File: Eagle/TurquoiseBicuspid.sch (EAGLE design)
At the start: 7 parts

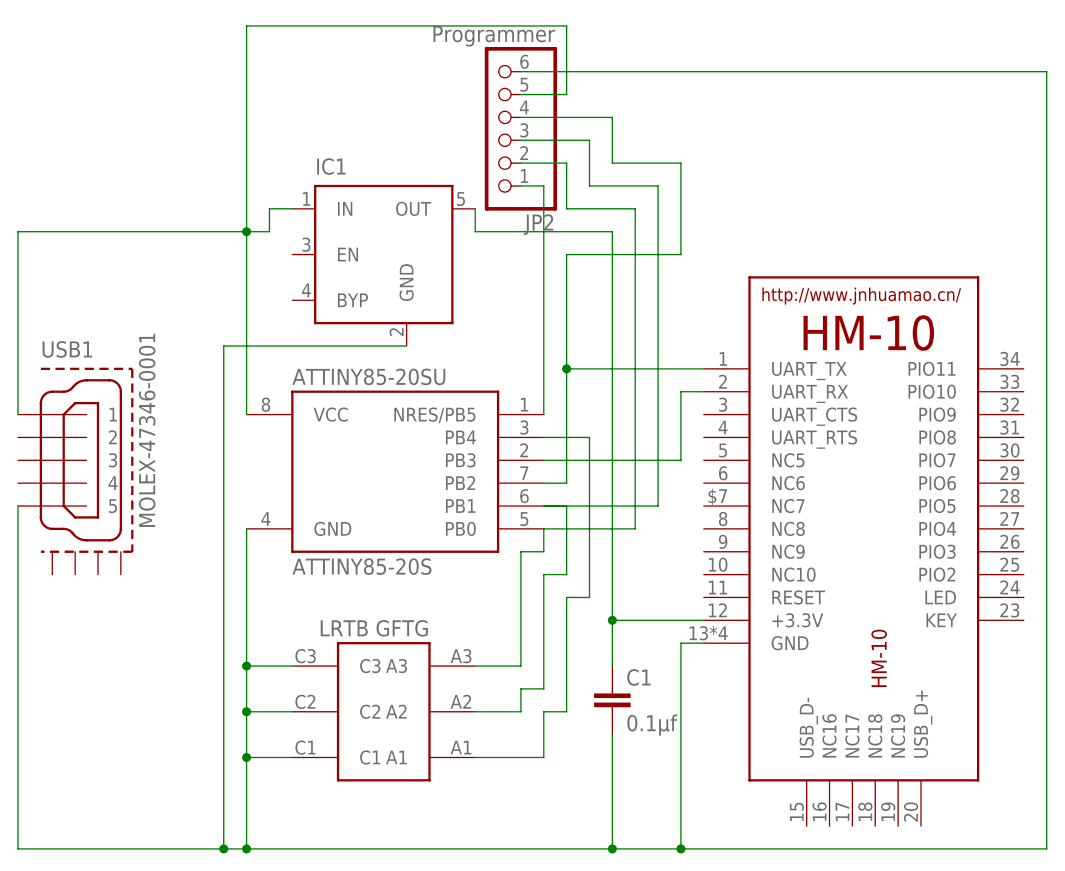
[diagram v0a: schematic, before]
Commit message: added resistors and switches
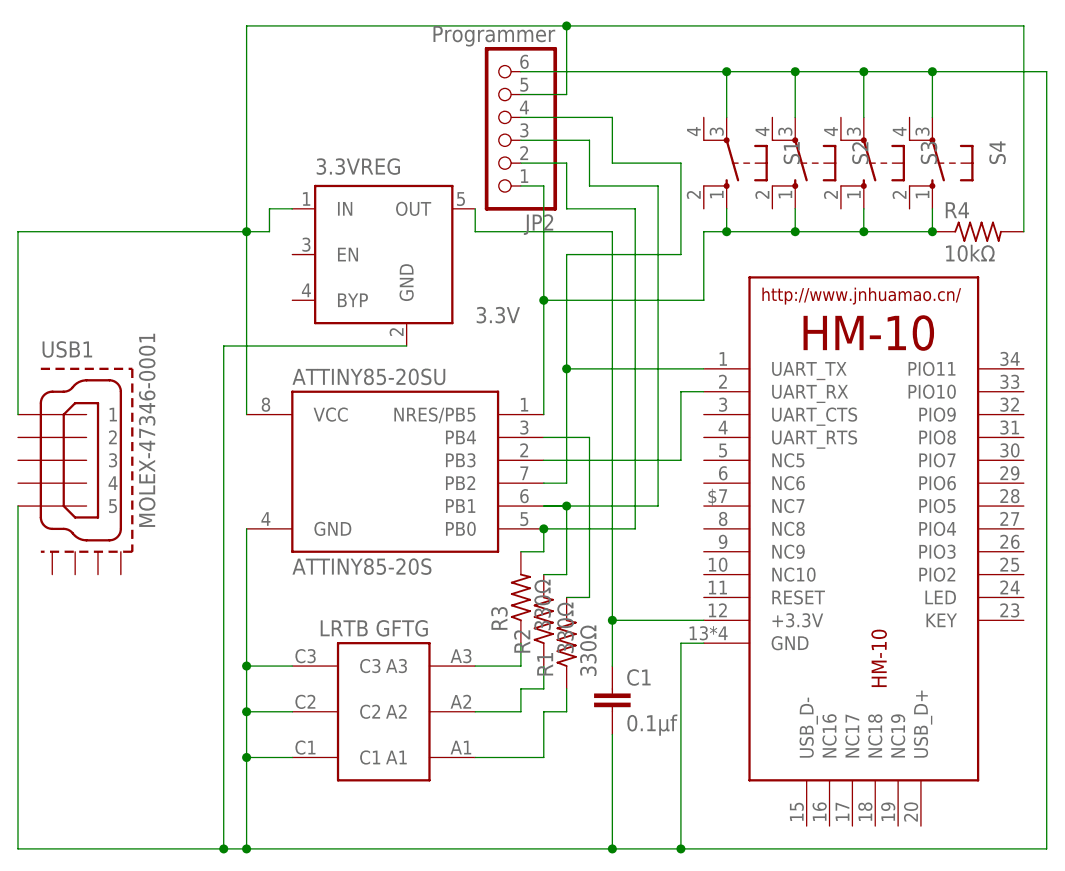
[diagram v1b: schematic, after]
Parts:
- added R1, R2, R3: 330Ω, rcl:R-US_M1206
- added R4: 10kΩ, rcl:R-US_R1206
- added S1, S2, S3, S4: (no value), switch-omron:10-XX
- 3.3VREG: value (none) -> 3.3V
- renumbered IC1 to 3.3VREG
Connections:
- new net N$7: R3.1, U$1.A3
- new net N$8: R2.1, U$1.A2
- new net N$9: R1.1, U$1.A1
- net 5V: now also R4.2
- net GND: now also S1.P, S2.P, S3.P, S4.P
- net N$1: now also R3.2; no longer U$1.A3
- net N$2: now also R2.2; no longer U$1.A2
- net N$3: now also R1.2; no longer U$1.A1
- net N$4: now also R4.1, S1.S, S2.S, S3.S, S4.S

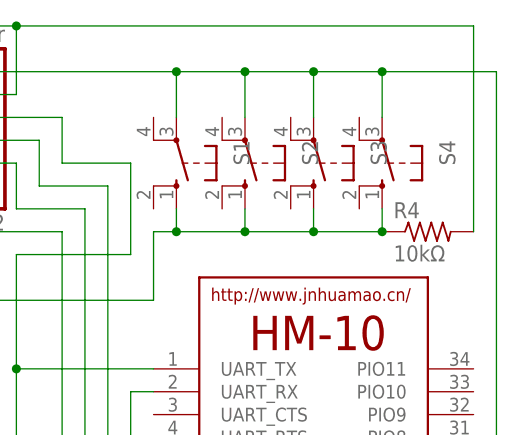
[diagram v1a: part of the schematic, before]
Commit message: removed 1 switch
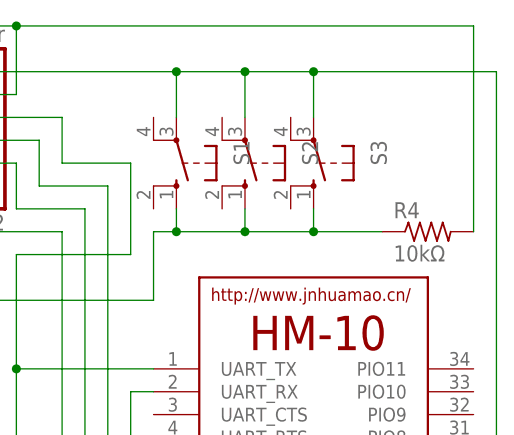
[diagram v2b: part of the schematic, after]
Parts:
- removed S4: (no value), switch-omron:10-XX
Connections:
- net GND: no longer S4.P
- net N$4: no longer S4.S
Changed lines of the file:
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@@
 <part name="S2" library="switch-omron" deviceset="10-XX" device=""/>
 <part name="S3" library="switch-omron" deviceset="10-XX" device=""/>
-<part name="S4" library="switch-omron" deviceset="10-XX" device=""/>
 </parts>
 <sheets>
@@
 <instance part="S2" gate="1" x="45.72" y="50.8" rot="R180"/>
 <instance part="S3" gate="1" x="53.34" y="50.8" rot="R180"/>
-<instance part="S4" gate="1" x="60.96" y="50.8" rot="R180"/>
 </instances>
 <busses>
@@
 <wire x1="38.1" y1="60.96" x2="45.72" y2="60.96" width="0.1524" layer="91"/>
 <wire x1="45.72" y1="60.96" x2="53.34" y2="60.96" width="0.1524" layer="91"/>
-<wire x1="53.34" y1="60.96" x2="60.96" y2="60.96" width="0.1524" layer="91"/>
-<wire x1="60.96" y1="60.96" x2="73.66" y2="60.96" width="0.1524" layer="91"/>
+<wire x1="53.34" y1="60.96" x2="73.66" y2="60.96" width="0.1524" layer="91"/>
 <wire x1="73.66" y1="60.96" x2="73.66" y2="-25.4" width="0.1524" layer="91"/>
 <pinref part="S1" gate="1" pin="P"/>
@@
 <pinref part="S3" gate="1" pin="P"/>
 <wire x1="53.34" y1="55.88" x2="53.34" y2="60.96" width="0.1524" layer="91"/>
-<pinref part="S4" gate="1" pin="P"/>
-<wire x1="60.96" y1="55.88" x2="60.96" y2="60.96" width="0.1524" layer="91"/>
 <junction x="38.1" y="60.96"/>
 <junction x="45.72" y="60.96"/>
 <junction x="53.34" y="60.96"/>
-<junction x="60.96" y="60.96"/>
 </segment>
 </net>
@@
 <pinref part="S3" gate="1" pin="S"/>
 <wire x1="53.34" y1="43.18" x2="53.34" y2="45.72" width="0.1524" layer="91"/>
-<pinref part="S4" gate="1" pin="S"/>
-<wire x1="60.96" y1="43.18" x2="60.96" y2="45.72" width="0.1524" layer="91"/>
-<junction x="60.96" y="43.18"/>
 <junction x="53.34" y="43.18"/>
 <junction x="45.72" y="43.18"/>

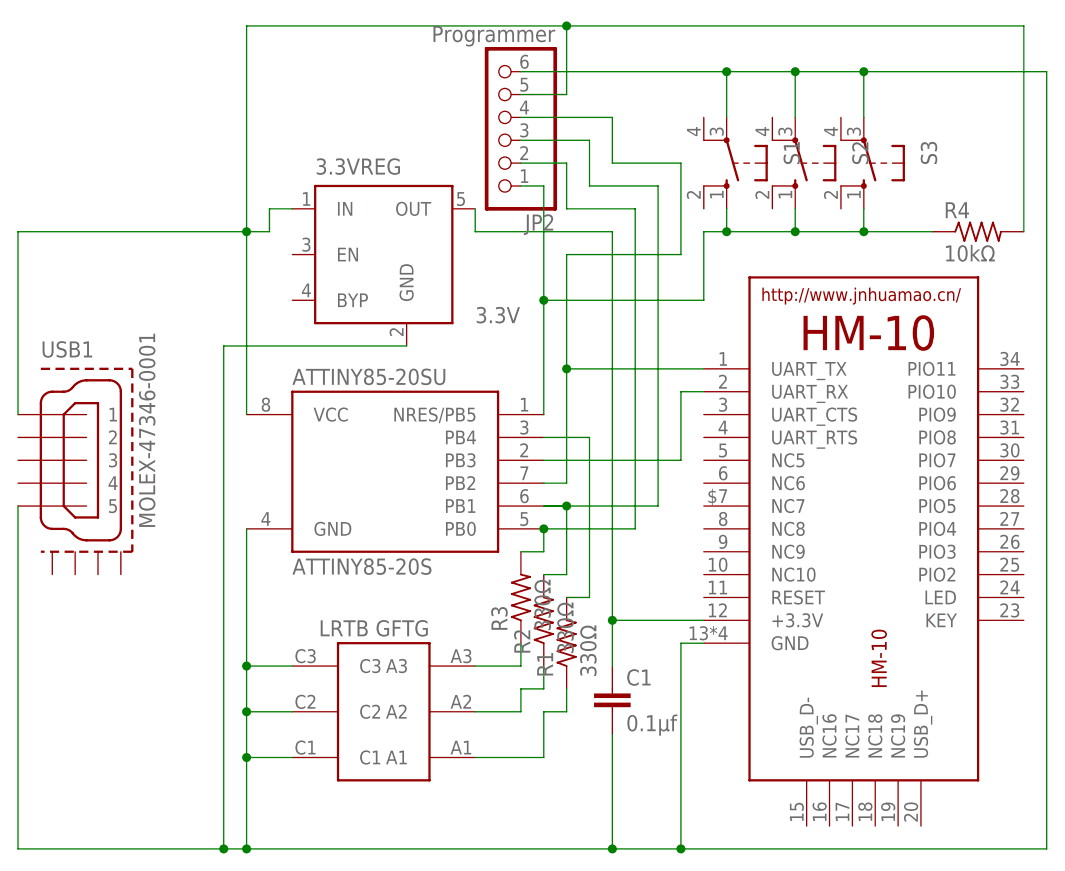
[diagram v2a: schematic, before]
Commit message: removed programming headers
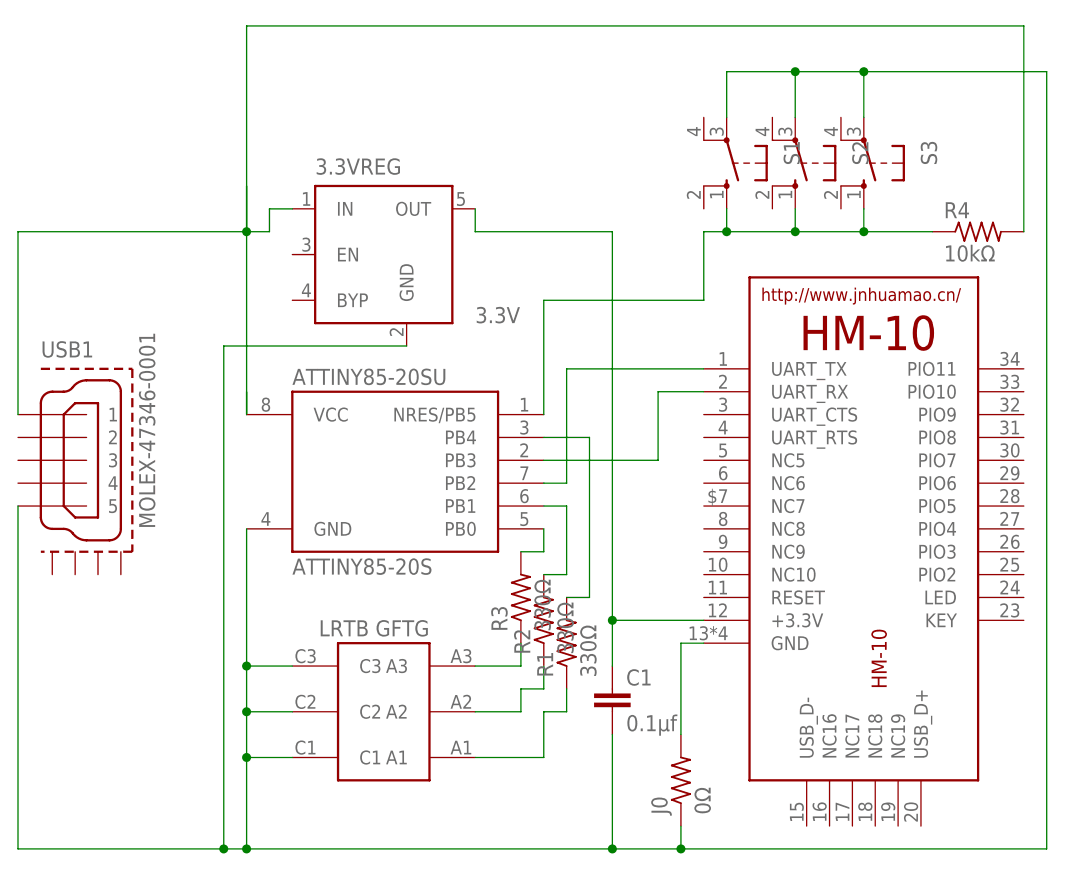
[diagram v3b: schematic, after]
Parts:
- removed JP2: Programmer, pinhead:PINHD-1X6
- added J0: 0Ω, rcl:R-US_R1206
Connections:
- removed net N$5 (its old number): ATTINY85-20SU.PB2, HM-10.UART_TX, JP2.4
- new net N$14: 3.3VREG.IN, USB1.1
- new net N$23: ATTINY85-20SU.PB2, HM-10.UART_TX
- new net N$6: HM-10.GND, J0.2
- net 5V: no longer 3.3VREG.IN, JP2.5, USB1.1
- net GND: now also J0.1; no longer HM-10.GND, JP2.6
- net N$1: no longer JP2.2
- net N$2: no longer JP2.3
- net N$4: no longer JP2.1

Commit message: fixed 5v
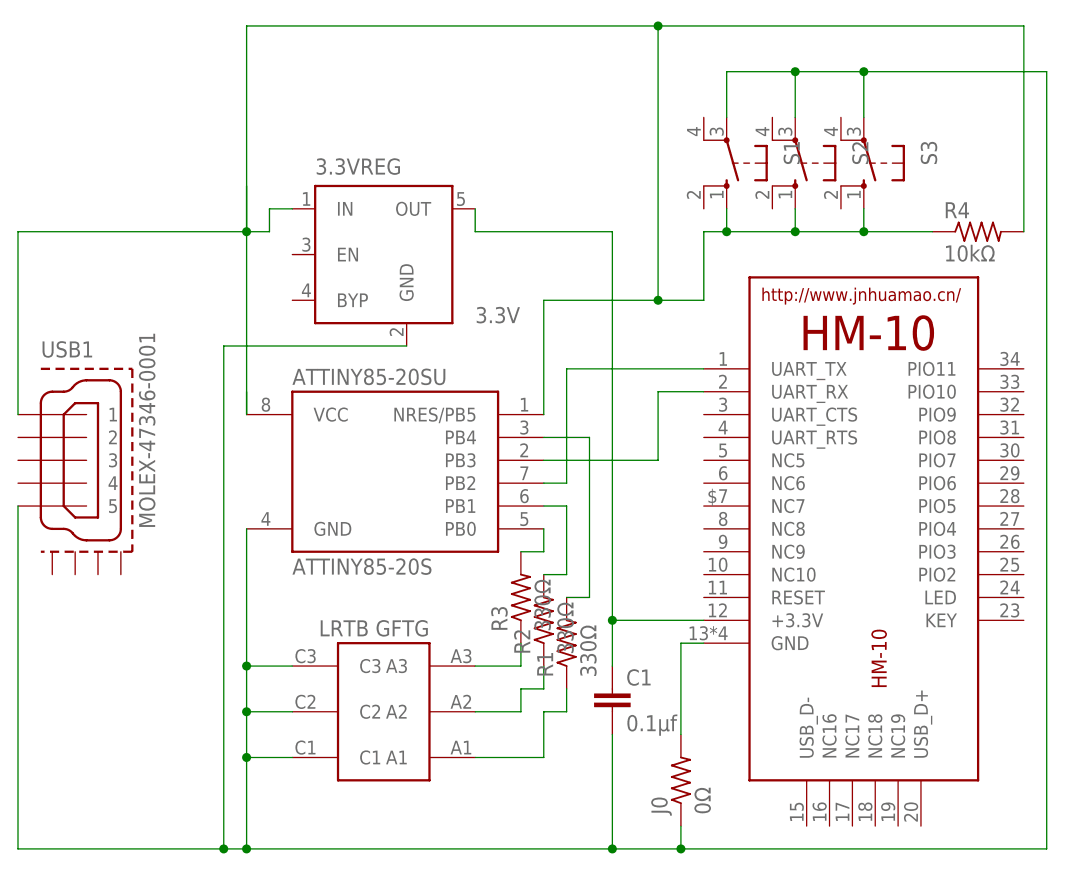
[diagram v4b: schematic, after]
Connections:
- removed net N$14: 3.3VREG.IN, USB1.1
- removed net N$4: ATTINY85-20SU.NRES/PB5, R4.1, S1.S, S2.S, S3.S
- net 5V: now also 3.3VREG.IN, ATTINY85-20SU.NRES/PB5, R4.1, S1.S, S2.S, S3.S, USB1.1
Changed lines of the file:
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@@
 <net name="5V" class="0">
 <segment>
-<wire x1="-15.24" y1="66.04" x2="71.12" y2="66.04" width="0.1524" layer="91"/>
+<wire x1="-15.24" y1="66.04" x2="30.48" y2="66.04" width="0.1524" layer="91"/>
+<wire x1="30.48" y1="66.04" x2="71.12" y2="66.04" width="0.1524" layer="91"/>
 <wire x1="71.12" y1="43.18" x2="71.12" y2="66.04" width="0.1524" layer="91"/>
 <pinref part="R4" gate="G$1" pin="2"/>
@@
 <wire x1="-15.24" y1="22.86" x2="-15.24" y2="25.4" width="0.1524" layer="91"/>
 <wire x1="-15.24" y1="66.04" x2="-15.24" y2="22.86" width="0.1524" layer="91"/>
+<junction x="30.48" y="66.04"/>
+<pinref part="ATTINY85-20SU" gate="G$1" pin="NRES/PB5"/>
+<wire x1="35.56" y1="35.56" x2="35.56" y2="43.18" width="0.1524" layer="91"/>
+<wire x1="35.56" y1="35.56" x2="30.48" y2="35.56" width="0.1524" layer="91"/>
+<wire x1="30.48" y1="35.56" x2="17.78" y2="35.56" width="0.1524" layer="91"/>
+<wire x1="17.78" y1="35.56" x2="17.78" y2="22.86" width="0.1524" layer="91"/>
+<pinref part="R4" gate="G$1" pin="1"/>
+<wire x1="60.96" y1="43.18" x2="53.34" y2="43.18" width="0.1524" layer="91"/>
+<wire x1="53.34" y1="43.18" x2="45.72" y2="43.18" width="0.1524" layer="91"/>
+<wire x1="45.72" y1="43.18" x2="38.1" y2="43.18" width="0.1524" layer="91"/>
+<pinref part="S2" gate="1" pin="S"/>
+<wire x1="38.1" y1="43.18" x2="35.56" y2="43.18" width="0.1524" layer="91"/>
+<wire x1="45.72" y1="43.18" x2="45.72" y2="45.72" width="0.1524" layer="91"/>
+<pinref part="S3" gate="1" pin="S"/>
+<wire x1="53.34" y1="43.18" x2="53.34" y2="45.72" width="0.1524" layer="91"/>
+<junction x="53.34" y="43.18"/>
+<junction x="45.72" y="43.18"/>
+<pinref part="S1" gate="1" pin="S"/>
+<wire x1="38.1" y1="45.72" x2="38.1" y2="43.18" width="0.1524" layer="91"/>
+<junction x="38.1" y="43.18"/>
+<junction x="30.48" y="35.56"/>
+<wire x1="30.48" y1="66.04" x2="30.48" y2="35.56" width="0.1524" layer="91"/>
+</segment>
+<segment>
+<pinref part="3.3VREG" gate="G1" pin="IN"/>
+<wire x1="-12.7" y1="45.72" x2="-10.16" y2="45.72" width="0.1524" layer="91"/>
+<wire x1="-12.7" y1="43.18" x2="-12.7" y2="45.72" width="0.1524" layer="91"/>
+<junction x="-15.24" y="43.18"/>
+<wire x1="-15.24" y1="48.26" x2="-15.24" y2="43.18" width="0.1524" layer="91"/>
+<wire x1="-15.24" y1="43.18" x2="-12.7" y2="43.18" width="0.1524" layer="91"/>
+<pinref part="USB1" gate="G$1" pin="1"/>
+<wire x1="-40.64" y1="22.86" x2="-40.64" y2="43.18" width="0.1524" layer="91"/>
+<wire x1="-40.64" y1="43.18" x2="-15.24" y2="43.18" width="0.1524" layer="91"/>
 </segment>
 </net>
@@
 </segment>
 </net>
-<net name="N$4" class="0">
-<segment>
-<pinref part="ATTINY85-20SU" gate="G$1" pin="NRES/PB5"/>
-<wire x1="35.56" y1="35.56" x2="35.56" y2="43.18" width="0.1524" layer="91"/>
-<wire x1="35.56" y1="35.56" x2="17.78" y2="35.56" width="0.1524" layer="91"/>
-<wire x1="17.78" y1="35.56" x2="17.78" y2="22.86" width="0.1524" layer="91"/>
-<pinref part="R4" gate="G$1" pin="1"/>
-<wire x1="60.96" y1="43.18" x2="53.34" y2="43.18" width="0.1524" layer="91"/>
-<wire x1="53.34" y1="43.18" x2="45.72" y2="43.18" width="0.1524" layer="91"/>
-<wire x1="45.72" y1="43.18" x2="38.1" y2="43.18" width="0.1524" layer="91"/>
-<pinref part="S2" gate="1" pin="S"/>
-<wire x1="38.1" y1="43.18" x2="35.56" y2="43.18" width="0.1524" layer="91"/>
-<wire x1="45.72" y1="43.18" x2="45.72" y2="45.72" width="0.1524" layer="91"/>
-<pinref part="S3" gate="1" pin="S"/>
-<wire x1="53.34" y1="43.18" x2="53.34" y2="45.72" width="0.1524" layer="91"/>
-<junction x="53.34" y="43.18"/>
-<junction x="45.72" y="43.18"/>
-<pinref part="S1" gate="1" pin="S"/>
-<wire x1="38.1" y1="45.72" x2="38.1" y2="43.18" width="0.1524" layer="91"/>
-<junction x="38.1" y="43.18"/>
-</segment>
-</net>
 <net name="N$6" class="0">
 <segment>
@@
 </segment>
 </net>
-<net name="N$14" class="0">
-<segment>
-<pinref part="3.3VREG" gate="G1" pin="IN"/>
-<wire x1="-12.7" y1="45.72" x2="-10.16" y2="45.72" width="0.1524" layer="91"/>
-<wire x1="-12.7" y1="43.18" x2="-12.7" y2="45.72" width="0.1524" layer="91"/>
-<junction x="-15.24" y="43.18"/>
-<wire x1="-15.24" y1="48.26" x2="-15.24" y2="43.18" width="0.1524" layer="91"/>
-<wire x1="-15.24" y1="43.18" x2="-12.7" y2="43.18" width="0.1524" layer="91"/>
-<pinref part="USB1" gate="G$1" pin="1"/>
-<wire x1="-40.64" y1="22.86" x2="-40.64" y2="43.18" width="0.1524" layer="91"/>
-<wire x1="-40.64" y1="43.18" x2="-15.24" y2="43.18" width="0.1524" layer="91"/>
-</segment>
-</net>
